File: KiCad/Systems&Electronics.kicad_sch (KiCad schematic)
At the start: 39 parts, among them U13 AD8495, U14 AD8495, U15 AD8495, U16 AD8495, U3 MAX485E, U4 MAX485E

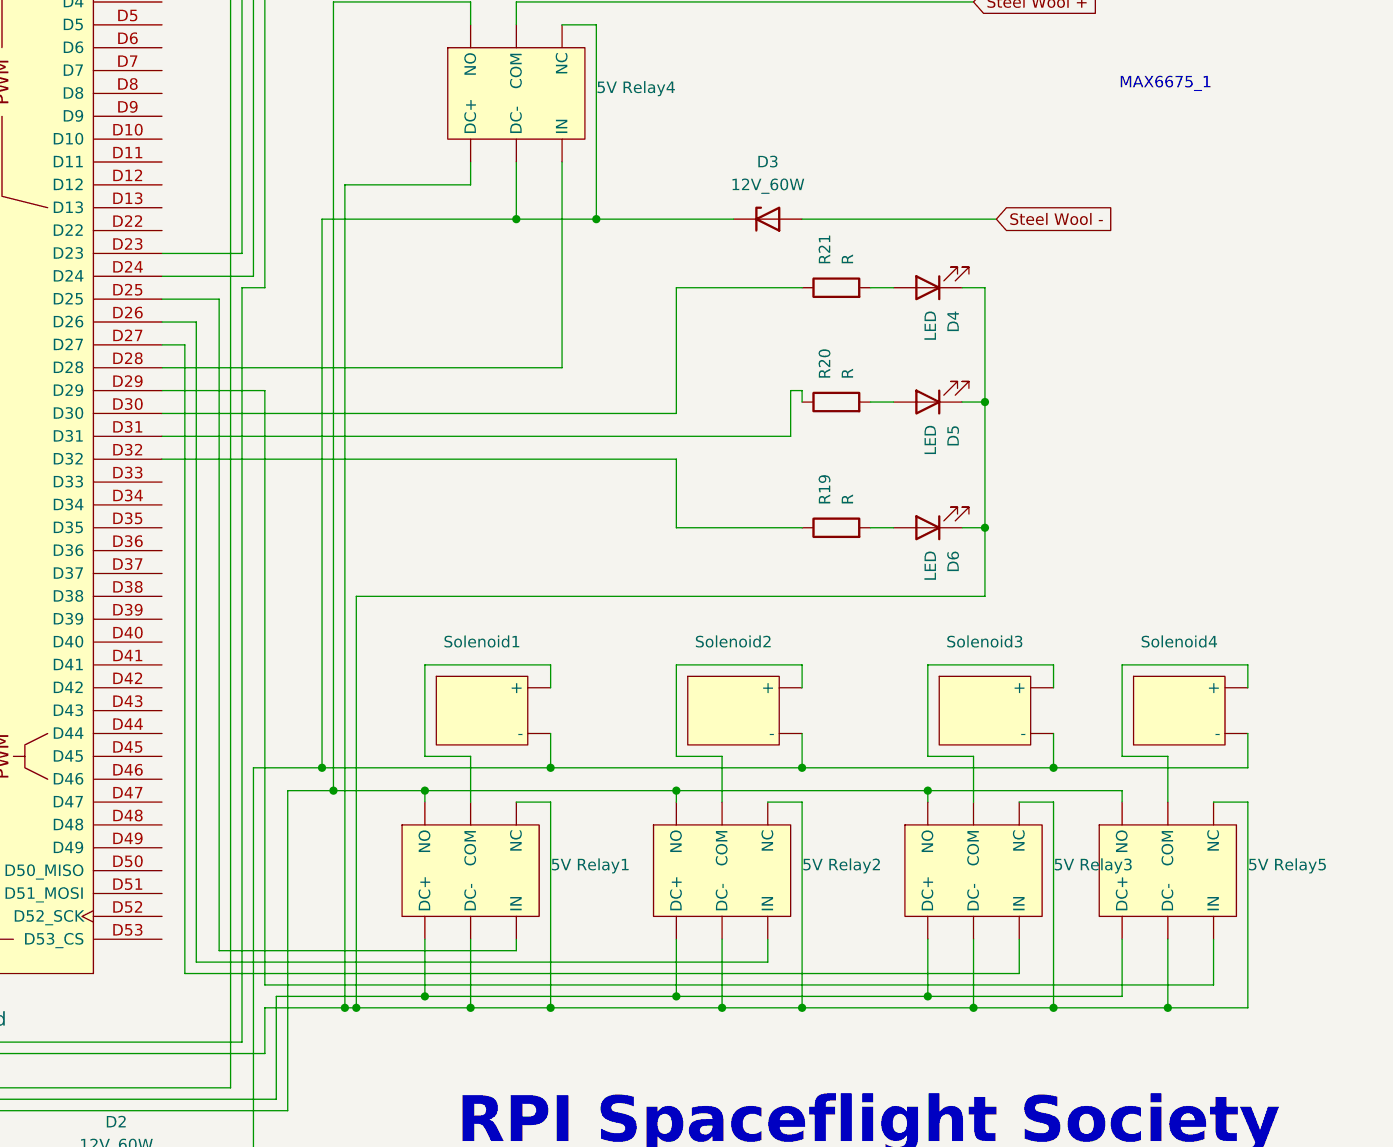
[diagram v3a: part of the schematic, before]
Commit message: feat(GUI) Command Reader/Writer Implementation and Starting PCB
* feat(GUI): starting coms)

* feat(comms): serial writer implementation v1

* feat(comms): integrate serial writer into main thread

* feat(comms): shutdown logic added

* Command Writer v2

* feat(comms): data send is partially working

* feat(comms): Serial Command Writer v4 started

* feat(comms): error handling and worker mainloop

* feat(comms): error handling and worker mainloop

* feat(comms): Serial Communications system v4 done

Needs to be connected to the main file properly
Needs to be tested

* feat(GUI): minor fixes

* feat(GUI): starting log handler

* feat(GUI): data and event logger untested

* feat(comms): connecting mainwindow to serial worker

* remove the need for metric data conversion

* feat(GUI): data logging fix, user alerts, and minor refactor of connections

* fix(GUI): update the names of the chart to adjust for the new sensor placement

* feat(GUI): UI should update when it receives new data.

TODO: needs to color the text boxes depending on whether data is in spec

* fix(GUI): fix build and remove extraneous logs

* feat(GUI): first iteration of the engine state machine

* updating firmware and schematics to be consistent

* Firmware Refactor (Untested)

* Firmware V1.2 Done

* Firmware V1.2 Done

* Implemented FSM for handling engine state.

TODO:
- Ability to create new log files when the test is restarted
- Clearing the graphs when a test is restarted
- QT Signal and Slot Connections
- Debugging

* Finished First Implementation

TODO: Testing, Debugging, and More Testing

* Fixing Window Size

* minor bug fixes

The arduino is not responding to the commands despite the RX LED
lighting up.

* Fixing Bugs with Comms

- Slowly making progress still lots to fix

* Fixed a ton of bugs. Software is getting close to completion.

- Still need to test data ingest
- Some of the failsafes seem to not be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
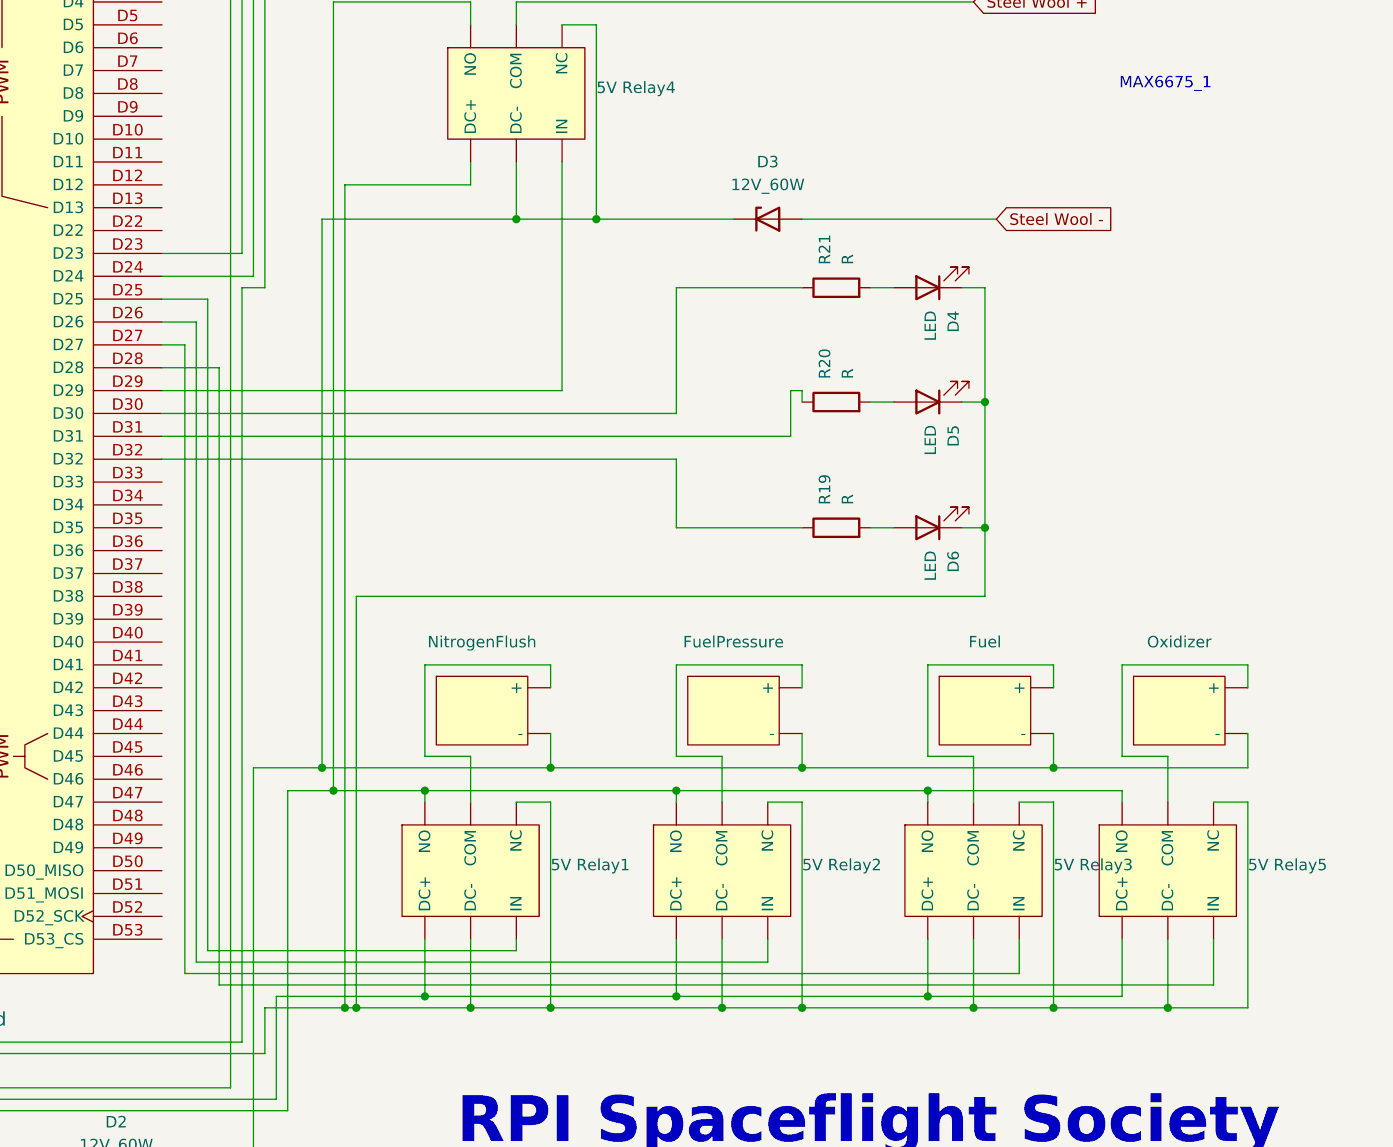
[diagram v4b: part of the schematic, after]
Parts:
- renumbered Solenoid3 to Fuel, Solenoid2 to FuelPressure, Solenoid1 to NitrogenFlush, Solenoid4 to Oxidizer
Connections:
- net at A1.D29: now also 5V Relay4. (NO); no longer 5V Relay5. (NO)
- net at Oxidizer. (-): now also 5V Relay4. (NO), D2.2 (A), D3.1 (K), Fuel. (-), FuelPressure. (-), NitrogenFlush. (-); no longer 5V Relay5. (NO)
- net at Pressure_Transducer1. (VCC), Pressure_Transducer2. (VCC), Pressure_Transducer3. (VCC)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: now also A1.GND1 (GND); no longer A1.5V3 (5V)
- net at A1.D28: now also 5V Relay5. (NO); no longer 5V Relay4. (NO)
- new net: 5V Relay1. (NO), 5V Relay2. (NO), 5V Relay3. (NO), 5V Relay4. (NO), 5V Relay5. (NO), A1.GND5 (GND), D4.1 (K), D5.1 (K), D6.1 (K)
- new net: 5V Relay1. (NO), 5V Relay2. (NO), 5V Relay3. (NO), 5V Relay5. (NO), A1.5V4 (5V)
- new net: 5V Relay5. (NO), Oxidizer. (-)
- new net: 5V Relay1. (NO), NitrogenFlush. (-)
- new net: A1.5V3 (5V), Pressure_Transducer1. (VCC), Pressure_Transducer2. (VCC), Pressure_Transducer3. (VCC), Pressure_Transducer4. (VCC), Pressure_Transducer5. (VCC), Pressure_Transducer6. (VCC)
- new net: HX711_Board1. (VCC), Load_Cell1. (VCC) (x3)
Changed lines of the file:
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@@
 	(wire
 		(pts
-			(xy 276.86 153.67) (xy 276.86 158.75)
+			(xy 276.86 158.75) (xy 276.86 153.67)
 		)
 		(stroke
@@
 	(wire
 		(pts
-			(xy 204.47 67.31) (xy 204.47 90.17)
-		)
-		(stroke
-			(width 0)
-			(type default)
-		)
-	)
-	(wire
-		(pts
 			(xy 49.53 156.21) (xy 49.53 166.37)
 		)
@@
 	(wire
 		(pts
-			(xy 276.86 158.75) (xy 171.45 158.75)
+			(xy 276.86 158.75) (xy 166.37 158.75)
 		)
 		(stroke
@@
 	(wire
 		(pts
-			(xy 166.37 82.55) (xy 160.02 82.55)
+			(xy 165.1 82.55) (xy 160.02 82.55)
 		)
 		(stroke
@@
 	(wire
 		(pts
+			(xy 166.37 90.17) (xy 160.02 90.17)
+		)
+		(stroke
+			(width 0)
+			(type default)
+		)
+	)
+	(wire
+		(pts
 			(xy 240.03 41.91) (xy 278.13 41.91)
 		)
@@
 	(wire
 		(pts
+			(xy 204.47 67.31) (xy 204.47 92.71)
+		)
+		(stroke
+			(width 0)
+			(type default)
+		)
+	)
+	(wire
+		(pts
 			(xy 173.99 172.72) (xy 173.99 137.16)
 		)
@@
 	(wire
 		(pts
-			(xy 199.39 154.94) (xy 166.37 154.94)
+			(xy 199.39 154.94) (xy 165.1 154.94)
 		)
 		(stroke
@@
 	(wire
 		(pts
+			(xy 204.47 92.71) (xy 160.02 92.71)
+		)
+		(stroke
+			(width 0)
+			(type default)
+		)
+	)
+	(wire
+		(pts
 			(xy 132.08 180.34) (xy 132.08 185.42)
 		)
@@
 	(wire
 		(pts
-			(xy 166.37 154.94) (xy 166.37 82.55)
+			(xy 165.1 154.94) (xy 165.1 82.55)
 		)
 		(stroke
@@
 	(wire
 		(pts
-			(xy 204.47 90.17) (xy 160.02 90.17)
-		)
-		(stroke
-			(width 0)
-			(type default)
-		)
-	)
-	(wire
-		(pts
 			(xy 12.7 104.14) (xy 12.7 118.11)
 		)
@@
 	(wire
 		(pts
-			(xy 171.45 92.71) (xy 160.02 92.71)
-		)
-		(stroke
-			(width 0)
-			(type default)
-		)
-	)
-	(wire
-		(pts
 			(xy 71.12 97.79) (xy 93.98 97.79)
 		)
@@
 	(wire
 		(pts
-			(xy 171.45 158.75) (xy 171.45 92.71)
+			(xy 166.37 90.17) (xy 166.37 158.75)
 		)
 		(stroke
@@
 	)
 	(symbol
+		(lib_name "Solenoids:Solenoid")
 		(lib_id "Solenoids:Solenoid")
 		(at 273.05 128.27 0)
@@
 		(dnp no)
 		(fields_autoplaced yes)
-		(property "Reference" "Solenoid4"
+		(property "Reference" "Oxidizer"
 			(at 273.05 120.65 0)
 			(effects
@@
 			(project "Systems&Electronics"
 				(path "/4e05caf8-77e4-4a22-9a05-51fcca8e50ff"
-					(reference "Solenoid4")
+					(reference "Oxidizer")
 					(unit 1)
 				)
@@
 	)
 	(symbol
+		(lib_name "Solenoids:Solenoid")
 		(lib_id "Solenoids:Solenoid")
 		(at 251.46 128.27 0)
@@
 		(dnp no)
 		(fields_autoplaced yes)
-		(property "Reference" "Solenoid3"
+		(property "Reference" "Fuel"
 			(at 251.46 120.65 0)
 			(effects
@@
 			(project ""
 				(path "/4e05caf8-77e4-4a22-9a05-51fcca8e50ff"
-					(reference "Solenoid3")
+					(reference "Fuel")
 					(unit 1)
 				)
@@
 	)
 	(symbol
+		(lib_name "Solenoids:Solenoid")
 		(lib_id "Solenoids:Solenoid")
 		(at 195.58 128.27 0)
@@
 		(dnp no)
 		(fields_autoplaced yes)
-		(property "Reference" "Solenoid1"
+		(property "Reference" "NitrogenFlush"
 			(at 195.58 120.65 0)
 			(effects
@@
 			(project ""
 				(path "/4e05caf8-77e4-4a22-9a05-51fcca8e50ff"
-					(reference "Solenoid1")
+					(reference "NitrogenFlush")
 					(unit 1)
 				)
@@
 	)
 	(symbol
+		(lib_name "Solenoids:Solenoid")
 		(lib_id "Solenoids:Solenoid")
 		(at 223.52 128.27 0)
@@
 		(dnp no)
 		(fields_autoplaced yes)
-		(property "Reference" "Solenoid2"
+		(property "Reference" "FuelPressure"
 			(at 223.52 120.65 0)
 			(effects
@@
 			(project ""
 				(path "/4e05caf8-77e4-4a22-9a05-51fcca8e50ff"
-					(reference "Solenoid2")
+					(reference "FuelPressure")
 					(unit 1)
 				)

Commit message: PCB Layout V1
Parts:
- removed D1, D2, D3: 12V_60W, Diode_SMD:Nexperia_DSN1608-2_1.6x0.8mm, symbol Diode:PTVS12VZ1USK
- removed D4, D5, D6: LED, symbol Device:LED
- removed D7, D8: D, symbol Device:D
- removed Fuel, FuelPressure, NitrogenFlush, Oxidizer: ~, symbol Solenoids:Solenoid
- removed Load_Cell1: ~, symbol Sensors:Load_Cell
- removed Pressure_Transducer1, Pressure_Transducer2, Pressure_Transducer3, Pressure_Transducer4, Pressure_Transducer5, Pressure_Transducer6: ~, symbol Sensors:Pressure_Transducer
- removed R19, R20, R21: R, symbol Device:R
- removed Thermocouple10, Thermocouple11, Thermocouple12, Thermocouple9: ~, symbol Sensors:Thermocouple
- removed U13, U14, U15, U16: AD8495, Package_SO:MSOP-8_3x3mm_P0.65mm, symbol Sensor_Temperature:AD8495
- added 12V_Power1: 12V Power, TerminalBlock:TerminalBlock_bornier-2_P5.08mm, symbol Connector:Screw_Terminal_01x02
- added COMMS_GND1: GND, TerminalBlock:TerminalBlock_bornier-2_P5.08mm, symbol Connector:Screw_Terminal_01x02
- added D1, D2, D3, D7, D8, DF1, D_FP1, D_N1, D_OXY1: LED, LED_THT:LED_D3.0mm, symbol Device:LED
- added J1, J2, J3, J4, J5, J6: Pressure Transducer, TerminalBlock:TerminalBlock_bornier-3_P5.08mm, symbol Connector:Screw_Terminal_01x03
- added J12: Screw_Terminal_01x02, TerminalBlock:TerminalBlock_bornier-2_P5.08mm, symbol Connector:Screw_Terminal_01x02
- added J13: Screw_Terminal_01x03, TerminalBlock:TerminalBlock_bornier-3_P5.08mm, symbol Connector:Screw_Terminal_01x03
- added J_Fuel1: Fuel, TerminalBlock:TerminalBlock_bornier-2_P5.08mm, symbol Connector:Screw_Terminal_01x02
- added J_Ign1: Igniter, TerminalBlock:TerminalBlock_bornier-2_P5.08mm, symbol Connector:Screw_Terminal_01x02
- added J_N1: Nitrogen Valve, TerminalBlock:TerminalBlock_bornier-2_P5.08mm, symbol Connector:Screw_Terminal_01x02
- added J_Oxy1: Oxidizer, TerminalBlock:TerminalBlock_bornier-2_P5.08mm, symbol Connector:Screw_Terminal_01x02
- added J_Pres1: Fuel Pressuization, TerminalBlock:TerminalBlock_bornier-2_P5.08mm, symbol Connector:Screw_Terminal_01x02
- added J_Shut1: Shutdown Valve, TerminalBlock:TerminalBlock_bornier-2_P5.08mm, symbol Connector:Screw_Terminal_01x02
- added R7, R8, R9, RF1, R_FP1, R_N1, R_OXY1, R_SHUT1: R, Resistor_THT:R_Axial_DIN0204_L3.6mm_D1.6mm_P5.08mm_Horizontal, symbol Device:R
- added R_IGN1: R200, Resistor_THT:R_Axial_DIN0204_L3.6mm_D1.6mm_P5.08mm_Horizontal, symbol Device:R
- added R_IGN2: 10R 10W, Resistor_THT:R_Axial_Power_L48.0mm_W12.5mm_P55.88mm, symbol Device:R
- added Relay_Shutdown1: ~, ValveControl:Relay, symbol 5VRelay:5V_Relay
- added Thermocouple1, Thermocouple2, Thermocouple3, Thermocouple4: ~, Sensors:AD8495, symbol Sensors:AD8495_PCB
- A1: footprint PCM_arduino-library:Arduino_Mega2560_R3_Shield -> Arduino:Arduino_Mega2560_R3_Shield
- HX711_Board1: footprint (none) -> Sensors:HX711
- RX1: renamed from U3; value MAX485E -> RX_MAX485; footprint Package_SO:SOIC-8_3.9x4.9mm_P1.27mm -> Communications:RS485_Transceiver
- Relay_F1: renamed from 5V Relay3; footprint (none) -> ValveControl:Relay
- Relay_Fuel_Pres1: renamed from 5V Relay2; footprint (none) -> ValveControl:Relay
- Relay_Ign1: renamed from 5V Relay4; footprint (none) -> ValveControl:Relay
- Relay_N1: renamed from 5V Relay1; footprint (none) -> ValveControl:Relay
- Relay_Oxy1: renamed from 5V Relay5; footprint (none) -> ValveControl:Relay
- TX1: renamed from U4; value MAX485E -> TX_MAX485; footprint Package_SO:SOIC-8_3.9x4.9mm_P1.27mm -> Communications:RS485_Transceiver
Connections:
- net at A1.D28: now also R_OXY1.2; no longer Relay_Oxy1. (NO)
- net at A1.D25: now also R_N1.1; no longer Relay_N1. (NO)
- net at A1.D30: now also R_SHUT1.1
- net at A1.3V3 (3.3V): now also HX711_Board1.VCC; no longer HX711_Board1. (VCC)
- net at A1.5V1 (5V), RX1.8 (VCC), TX1.2 (~{RE})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: now also A1.5V3 (5V), A1.5V4 (5V), Relay_F1.DC+, Relay_Fuel_Pres1.DC+, Relay_Ign1.DC+, Relay_N1.DC+, Relay_Oxy1.DC+, J1.2 (Pin_2), J2.2 (Pin_2), J3.2 (Pin_2), J4.2 (Pin_2), J5.2 (Pin_2), J6.2 (Pin_2), Relay_Shutdown1.DC+, Thermocouple1.V+, Thermocouple2.V+, Thermocouple3.V+, Thermocouple4.V+
- net at A1.A0: now also J1.3 (Pin_3)
- net at A1.A1: now also J2.3 (Pin_3)
- net at A1.A2: now also J3.3 (Pin_3)
- net at A1.A3: now also J4.3 (Pin_3)
- net at A1.A4: now also J5.3 (Pin_3)
- net at A1.A5: now also J6.3 (Pin_3)
- net at A1.A6: now also Thermocouple1.OUT
- net at A1.A7: now also Thermocouple2.OUT
- net at A1.A8: now also Thermocouple3.OUT
- net at A1.A9: now also Thermocouple4.OUT
- net at A1.D18 (D18/TX1): now also TX1.4 (DI)
- net at A1.D19 (D19/RX1): now also RX1.1 (RO)
- net at A1.D23: now also HX711_Board1.SCK; no longer HX711_Board1. (VCC)
- net at A1.D24: now also HX711_Board1.DT; no longer HX711_Board1. (VCC)
- net at A1.D26: now also R_FP1.1; no longer Relay_Fuel_Pres1. (NO)
- net at A1.D27: now also RF1.2; no longer Relay_F1. (NO)
- net at A1.D29: now also R_IGN1.1; no longer Relay_Ign1. (NO)
- net at A1.D4: now also R7.1
- net at A1.D5: now also R8.1
- net at A1.D6: now also R9.1
- net at A1.GND1 (GND): now also A1.GND2 (GND), A1.GND3 (GND), A1.GND5 (GND), A1.GND6 (GND), HX711_Board1.GND, Relay_F1.DC-, Relay_F1.NC, Relay_Fuel_Pres1.DC-, Relay_Fuel_Pres1.NC, Relay_Ign1.DC-, Relay_Ign1.NC, Relay_N1.DC-, Relay_N1.NC, Relay_Oxy1.DC-, Relay_Oxy1.NC, 12V_Power1.1 (Pin_1), D1.1 (K), D2.1 (K), D3.1 (K), J1.1 (Pin_1), J13.1 (Pin_1), J2.1 (Pin_1), J3.1 (Pin_1), J4.1 (Pin_1), J5.1 (Pin_1), J6.1 (Pin_1), J_Fuel1.1 (Pin_1), J_Ign1.1 (Pin_1), J_N1.1 (Pin_1), J_Oxy1.1 (Pin_1), J_Pres1.1 (Pin_1), J_Shut1.1 (Pin_1), Relay_Shutdown1.DC-, Relay_Shutdown1.NC, Thermocouple1.GND, Thermocouple2.GND, Thermocouple3.GND, Thermocouple4.GND
- removed net +12V: A1.VIN, Relay_F1. (NO), Relay_Fuel_Pres1. (NO), Relay_Ign1. (NO), Relay_N1. (NO), Relay_Oxy1. (NO)
- net Comms GND: no longer names the net of RX1.2 (~{RE}), RX1.3 (DE), RX1.4 (DI), RX1.5 (GND), TX1.1 (RO), TX1.5 (GND)
- net Comms GND: now also COMMS_GND1.1 (Pin_1), COMMS_GND1.2 (Pin_2)
- removed net Steel Wool +: Relay_Ign1. (NO)
- new net: J_N1.2 (Pin_2), Relay_N1.COM
- new net: J_Oxy1.2 (Pin_2), Relay_Oxy1.COM
- new net: D_OXY1.1 (K), Relay_Oxy1.IN1
- new net: 12V_Power1.2 (Pin_2), A1.VIN, Relay_F1.NO, Relay_Fuel_Pres1.NO, Relay_Ign1.NO, Relay_N1.NO, Relay_Oxy1.NO, Relay_Shutdown1.NO
- new net: D7.2 (A), R_IGN1.2
- new net: D_N1.1 (K), Relay_N1.IN1
- new net: DF1.2 (A), RF1.1
- new net: D_FP1.1 (K), Relay_Fuel_Pres1.IN1
- new net: D_FP1.2 (A), R_FP1.2
- new net: D8.2 (A), R_SHUT1.2
- new net: D8.1 (K), Relay_Shutdown1.IN1
- new net: D1.2 (A), R7.2
- new net: J_Shut1.2 (Pin_2), Relay_Shutdown1.COM
- new net: D_N1.2 (A), R_N1.2
- new net: J_Pres1.2 (Pin_2), Relay_Fuel_Pres1.COM
- new net: D2.2 (A), R8.2
- new net: R_IGN2.1, Relay_Ign1.COM
- new net: D7.1 (K), Relay_Ign1.IN1
- new net: D3.2 (A), R9.2
- new net: HX711_Board1.E-, J12.1 (Pin_1)
- new net: HX711_Board1.E+, J12.2 (Pin_2)
- new net: J_Fuel1.2 (Pin_2), Relay_F1.COM
- new net: DF1.1 (K), Relay_F1.IN1
- new net: D_OXY1.2 (A), R_OXY1.1
- new net: HX711_Board1.A+, J13.3 (Pin_3)
- new net: HX711_Board1.A-, J13.2 (Pin_2)
- new net: J_Ign1.2 (Pin_2), R_IGN2.2
- no-connect marks 0 -> 60
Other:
- note added: "1.2.0"
- note added: "January 31, 2025"
- note removed: "1.1.0"
- note removed: "MAX6675_1"
- note removed: "September 10, 2024"
